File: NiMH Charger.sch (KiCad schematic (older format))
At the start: 23 parts, among them Q1 IRF510, Q2 IRF510, Q3 IRF510, Q4 IRF510, U1 Arduino_NANO, U2 LM7805

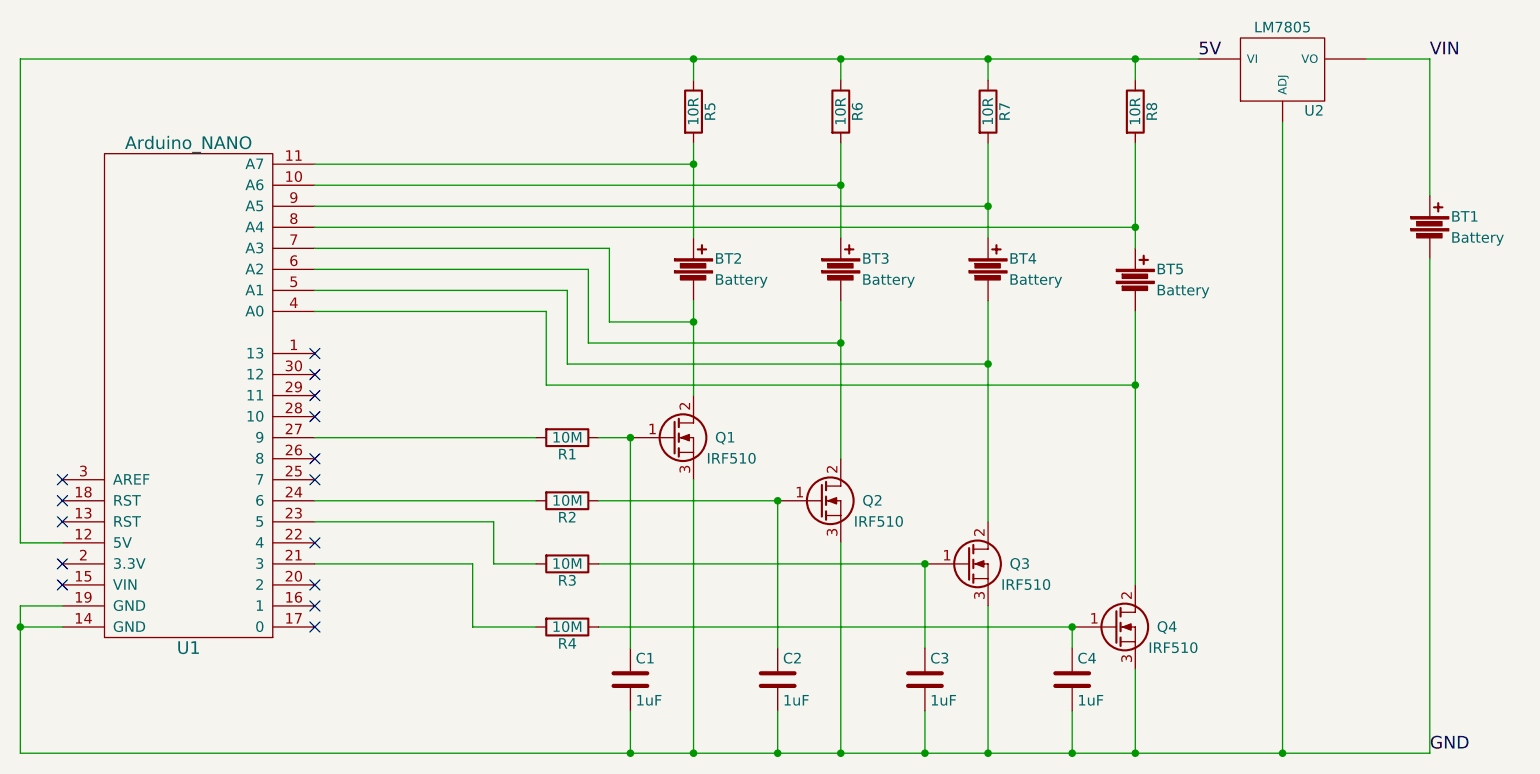
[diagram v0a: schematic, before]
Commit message: Removed 7805 Voltage Regulator
Unsure whether 7805 will be able to provide the necessary current should all four cells be charging simultaneously at highest current. The circuit now relies on a regulated 5V supply voltage.
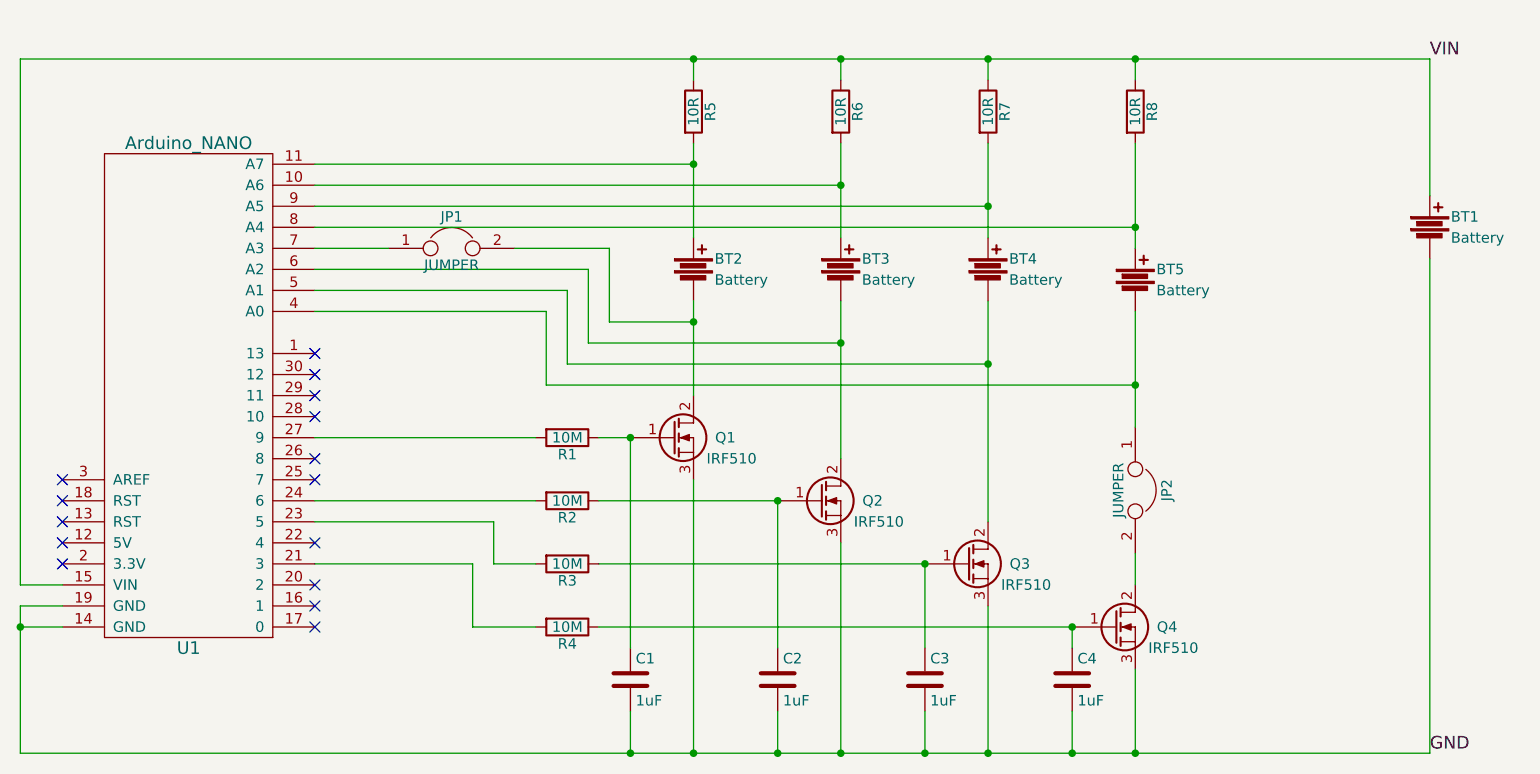
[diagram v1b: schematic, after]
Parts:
- removed U2: LM7805, TO_SOT_Packages_THT:TO-220_Neutral123_Vertical, symbol LM317
- added JP1, JP2: JUMPER, Custom:Jumper, symbol JUMPER
- R1, R2, R3, R4: footprint Discret:R1 -> Resistors_ThroughHole:Resistor_Horizontal_RM10mm
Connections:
- net VIN: now also R5.1, R6.1, R7.1, R8.1, U1.15 (VIN)
- net at BT2.2, Q1.2 (D): now also JP1.2; no longer U1.7 (A3)
- net at BT5.2, U1.4 (A0): now also JP2.1; no longer Q4.2 (D)
- removed net 5V: R5.1, R6.1, R7.1, R8.1, U1.12 (5V)
- new net: JP2.2, Q4.2 (D)
- new net: JP1.1, U1.7 (A3)
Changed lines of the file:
@@
 F 0 "R1" V 5480 3950 50  0000 C CNN
 F 1 "10M" V 5400 3950 50  0000 C CNN
-F 2 "Discret:R1" V 5330 3950 50  0001 C CNN
+F 2 "Resistors_ThroughHole:Resistor_Horizontal_RM10mm" V 5330 3950 50  0001 C CNN
 F 3 "" H 5400 3950 50  0000 C CNN
 	1    5400 3950
@@
 F 0 "R2" V 5480 4250 50  0000 C CNN
 F 1 "10M" V 5400 4250 50  0000 C CNN
-F 2 "Discret:R1" V 5330 4250 50  0001 C CNN
+F 2 "Resistors_ThroughHole:Resistor_Horizontal_RM10mm" V 5330 4250 50  0001 C CNN
 F 3 "" H 5400 4250 50  0000 C CNN
 	1    5400 4250
@@
 F 0 "R3" V 5480 4550 50  0000 C CNN
 F 1 "10M" V 5400 4550 50  0000 C CNN
-F 2 "Discret:R1" V 5330 4550 50  0001 C CNN
+F 2 "Resistors_ThroughHole:Resistor_Horizontal_RM10mm" V 5330 4550 50  0001 C CNN
 F 3 "" H 5400 4550 50  0000 C CNN
 	1    5400 4550
@@
 F 0 "R4" V 5480 4850 50  0000 C CNN
 F 1 "10M" V 5400 4850 50  0000 C CNN
-F 2 "Discret:R1" V 5330 4850 50  0001 C CNN
+F 2 "Resistors_ThroughHole:Resistor_Horizontal_RM10mm" V 5330 4850 50  0001 C CNN
 F 3 "" H 5400 4850 50  0000 C CNN
 	1    5400 4850
 	0    1    1    0
 $EndComp
-Text Label 8400 2150 0    60   ~ 0
-5V
 Text Label 9500 5450 0    60   ~ 0
 GND
@@
 Text Label 9500 2150 0    60   ~ 0
 VIN
-$Comp
-L LM317 U2
-U 1 1 57FD8759
-P 8800 2200
-F 0 "U2" H 8950 2004 50  0000 C CNN
-F 1 "LM7805" H 8800 2400 50  0000 C CNN
-F 2 "TO_SOT_Packages_THT:TO-220_Neutral123_Vertical" H 8800 2200 50  0001 C CNN
-F 3 "" H 8800 2200 50  0000 C CNN
-	1    8800 2200
-	1    0    0    -1
-$EndComp
 Wire Wire Line
 	4200 2950 8100 2950
@@
 	7800 4850 7800 4950
 Wire Wire Line
-	2800 2150 8400 2150
+	2800 2150 9500 2150
 Connection ~ 7400 2150
 Connection ~ 6700 2150
@@
 Wire Wire Line
 	5600 3400 5600 3050
-Wire Wire Line
-	5600 3050 4200 3050
 Connection ~ 6000 3400
 Wire Wire Line
@@
 Wire Wire Line
 	5400 3600 5400 3250
-Wire Wire Line
-	5400 3250 4200 3250
 Connection ~ 7400 3600
 Wire Wire Line
@@
 Connection ~ 6000 2150
 Wire Wire Line
-	8100 3350 8100 4650
-Wire Wire Line
-	9200 2150 9500 2150
-Wire Wire Line
-	8800 2450 8800 5450
-Connection ~ 8800 5450
-NoConn ~ 3000 4650
-Wire Wire Line
-	2800 2150 2800 4450
-Wire Wire Line
-	2800 4450 3000 4450
+	2800 2150 2800 4650
+Wire Wire Line
+	2800 4650 3000 4650
+NoConn ~ 3000 4450
+$Comp
+L JUMPER JP1
+U 1 1 585A9C0F
+P 4850 3050
+F 0 "JP1" H 4850 3200 50  0000 C CNN
+F 1 "JUMPER" H 4850 2970 50  0000 C CNN
+F 2 "Custom:Jumper" H 4850 3050 50  0001 C CNN
+F 3 "" H 4850 3050 50  0000 C CNN
+	1    4850 3050
+	1    0    0    -1
+$EndComp
+Wire Wire Line
+	4200 3050 4550 3050
+Wire Wire Line
+	5600 3050 5150 3050
+Wire Wire Line
+	5400 3250 4200 3250
+$Comp
+L JUMPER JP2
+U 1 1 585AAD63
+P 8100 4200
+F 0 "JP2" H 8100 4350 50  0000 C CNN
+F 1 "JUMPER" H 8100 4120 50  0000 C CNN
+F 2 "Custom:Jumper" H 8100 4200 50  0001 C CNN
+F 3 "" H 8100 4200 50  0000 C CNN
+	1    8100 4200
+	0    1    1    0
+$EndComp
+Wire Wire Line
+	8100 3350 8100 3900
+Wire Wire Line
+	8100 4500 8100 4650
 $EndSCHEMATC
